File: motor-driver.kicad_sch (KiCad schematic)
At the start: 0 parts

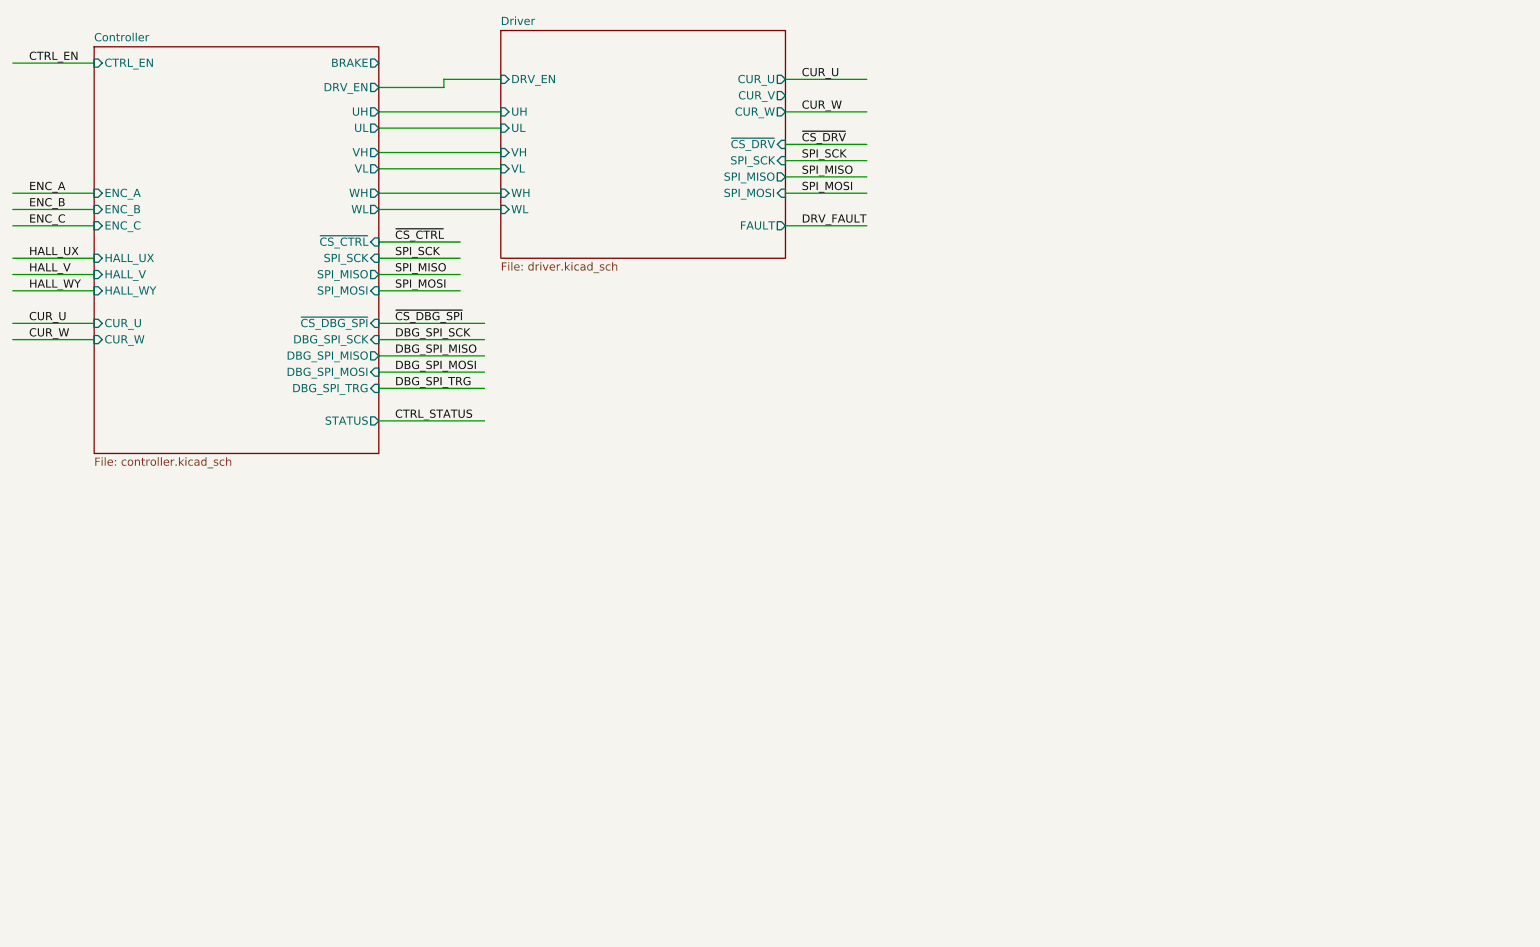
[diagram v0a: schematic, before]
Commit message: Add RTMI connector.
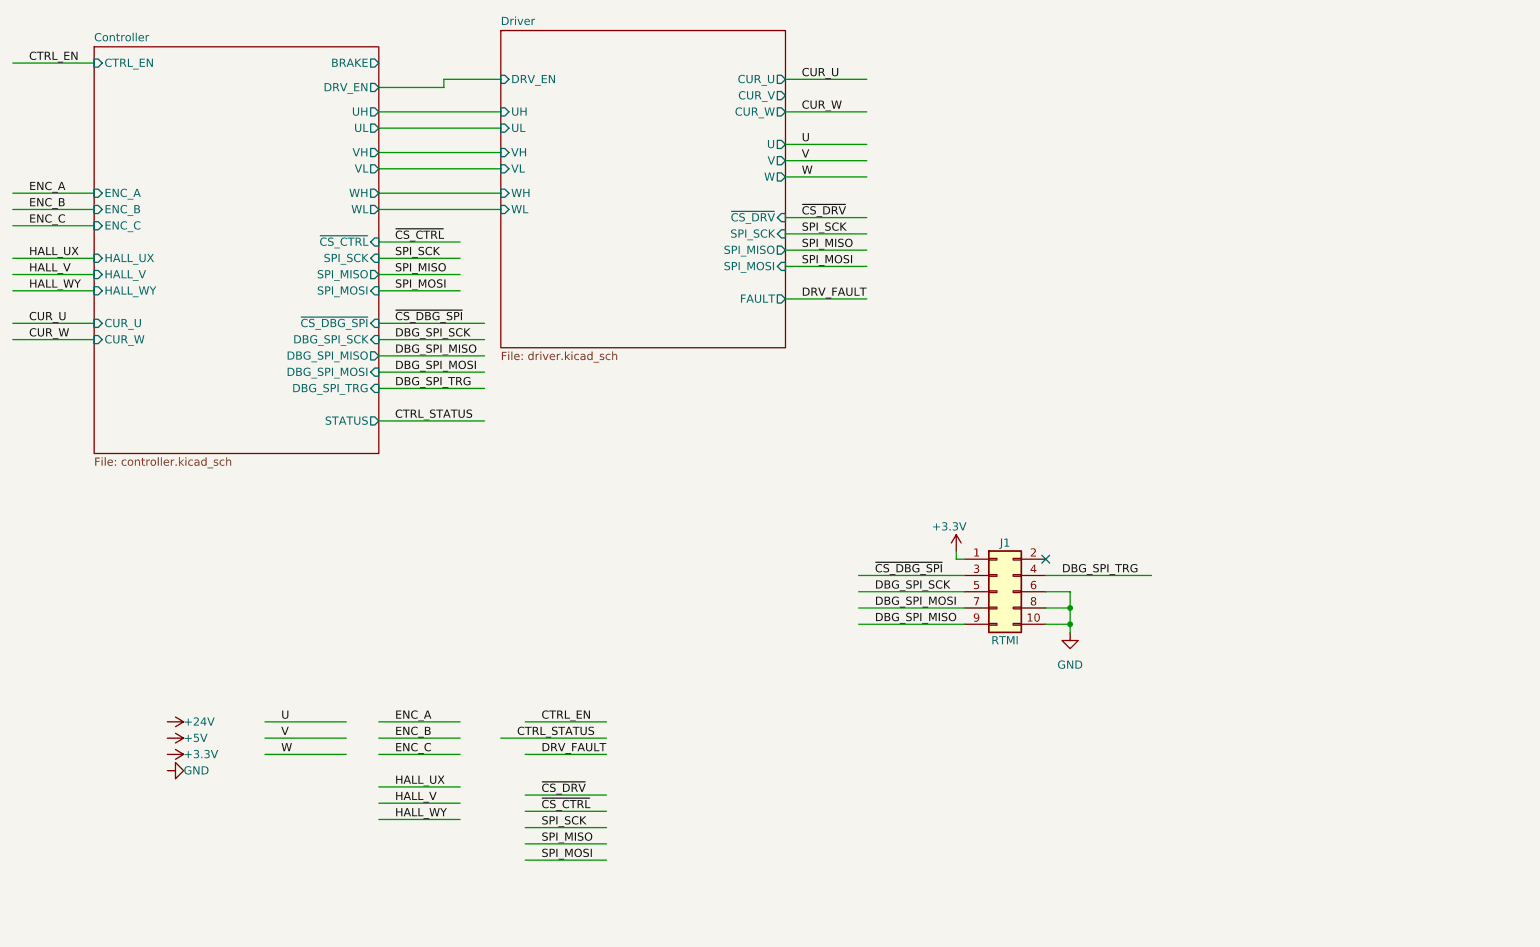
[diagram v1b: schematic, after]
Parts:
- added J1: RTMI, symbol Connector_Generic:Conn_02x05_Odd_Even
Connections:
- net DBG_SPI_MISO: now also J1.9 (Pin_9)
- net DBG_SPI_MOSI: now also J1.7 (Pin_7)
- net DBG_SPI_SCK: now also J1.5 (Pin_5)
- net DBG_SPI_TRG: now also J1.4 (Pin_4)
- net ~{CS_DBG_SPI}: now also J1.3 (Pin_3)
- new net +3.3V: J1.1 (Pin_1)
- new net GND: J1.10 (Pin_10), J1.6 (Pin_6), J1.8 (Pin_8)
- no-connect marks 0 -> 1
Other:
- sheet Driver ports: added U, V, W; removed none

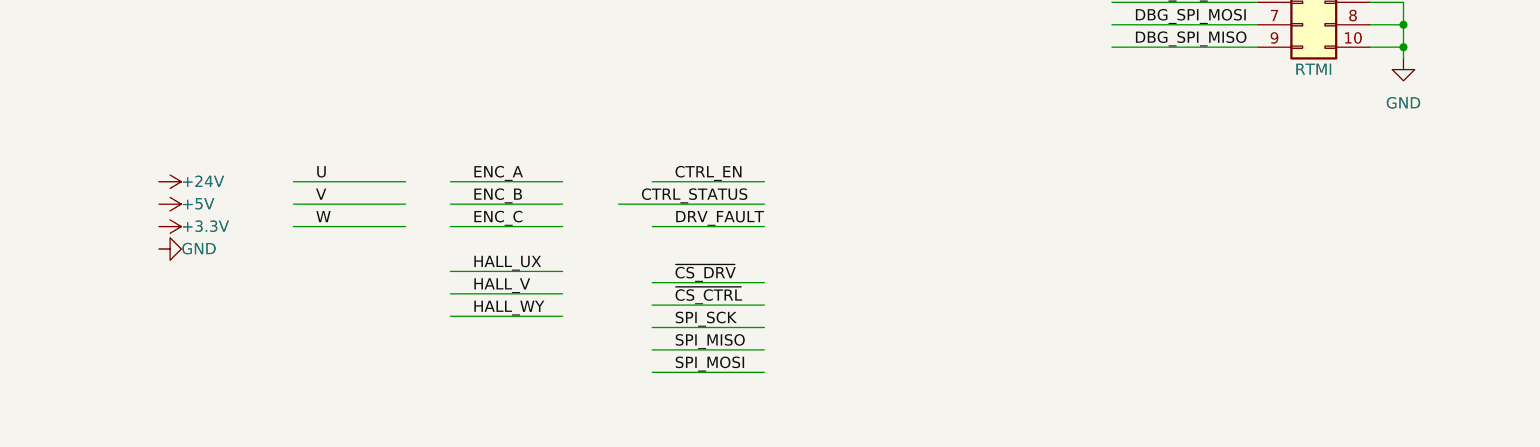
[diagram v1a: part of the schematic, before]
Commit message: Add stacking pin headers.
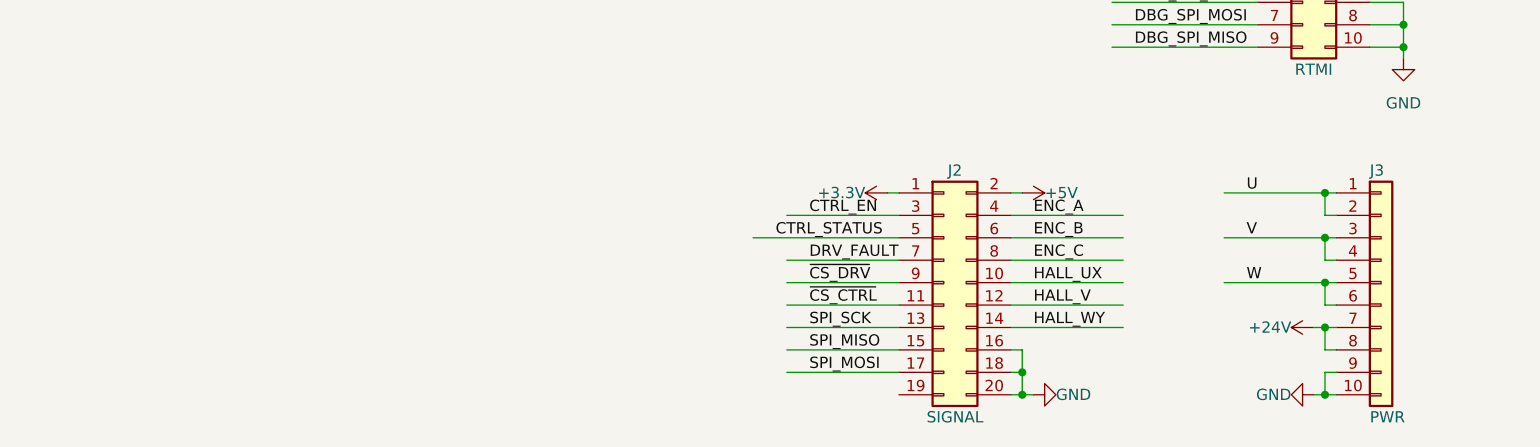
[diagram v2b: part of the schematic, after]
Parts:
- added J2: SIGNAL, Connector_PinHeader_2.54mm:PinHeader_2x10_P2.54mm_Vertical, symbol Connector_Generic:Conn_02x10_Odd_Even
- added J3: PWR, Connector_PinHeader_2.54mm:PinHeader_1x10_P2.54mm_Vertical, symbol Connector_Generic:Conn_01x10
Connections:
- net +24V: now also J3.7 (Pin_7), J3.8 (Pin_8)
- net +3.3V: now also J2.1 (Pin_1)
- net +5V: now also J2.2 (Pin_2)
- net CTRL_EN: now also J2.3 (Pin_3)
- net CTRL_STATUS: now also J2.5 (Pin_5)
- net DRV_FAULT: now also J2.7 (Pin_7)
- net ENC_A: now also J2.4 (Pin_4)
- net ENC_B: now also J2.6 (Pin_6)
- net ENC_C: now also J2.8 (Pin_8)
- net GND: now also J2.16 (Pin_16), J2.18 (Pin_18), J2.20 (Pin_20), J3.10 (Pin_10), J3.9 (Pin_9)
- net HALL_UX: now also J2.10 (Pin_10)
- net HALL_V: now also J2.12 (Pin_12)
- net HALL_WY: now also J2.14 (Pin_14)
- net SPI_MISO: now also J2.15 (Pin_15)
- net SPI_MOSI: now also J2.17 (Pin_17)
- net SPI_SCK: now also J2.13 (Pin_13)
- net U: now also J3.1 (Pin_1), J3.2 (Pin_2)
- net V: now also J3.3 (Pin_3), J3.4 (Pin_4)
- net W: now also J3.5 (Pin_5), J3.6 (Pin_6)
- net ~{CS_CTRL}: now also J2.11 (Pin_11)
- net ~{CS_DRV}: now also J2.9 (Pin_9)

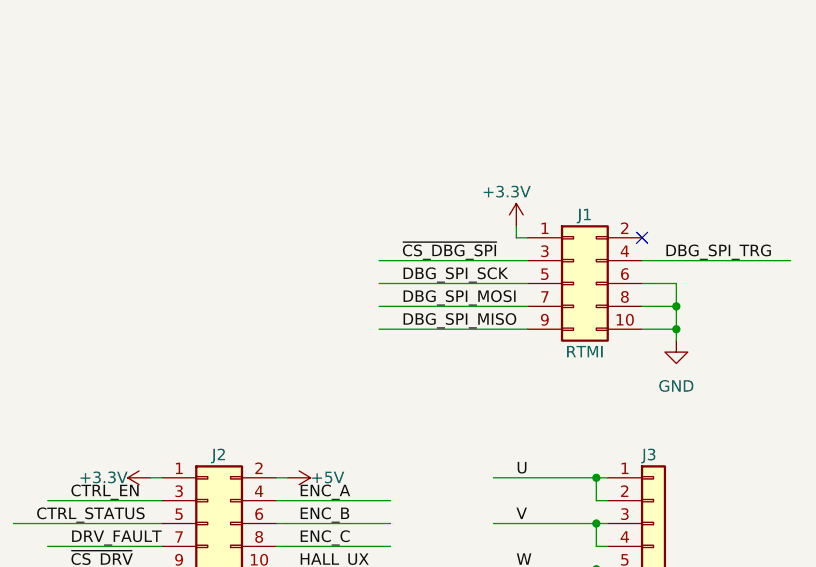
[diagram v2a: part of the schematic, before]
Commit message: Assign footprints and part numbers.
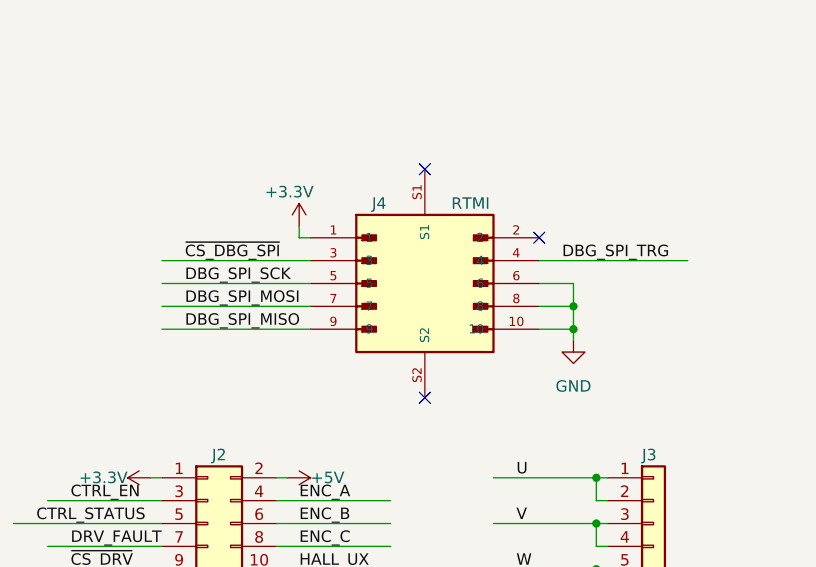
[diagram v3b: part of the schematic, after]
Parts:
- removed J1: RTMI, symbol Connector_Generic:Conn_02x05_Odd_Even
- added J4: RTMI, DF20EF-10DP-1V_52:HRS_DF20EF-10DP-1V(52), symbol DF20EF-10DP-1V_52_:DF20EF-10DP-1V(52)
- J2: MPN (none) -> 61302021121
- J3: MPN (none) -> 61301011121
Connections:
- net +3.3V: now also J4.1
- net DBG_SPI_MISO: now also J4.9
- net DBG_SPI_MOSI: now also J4.7
- net DBG_SPI_SCK: now also J4.5
- net DBG_SPI_TRG: now also J4.4
- net GND: now also J4.10, J4.6, J4.8
- net ~{CS_DBG_SPI}: now also J4.3
- no-connect marks 1 -> 3

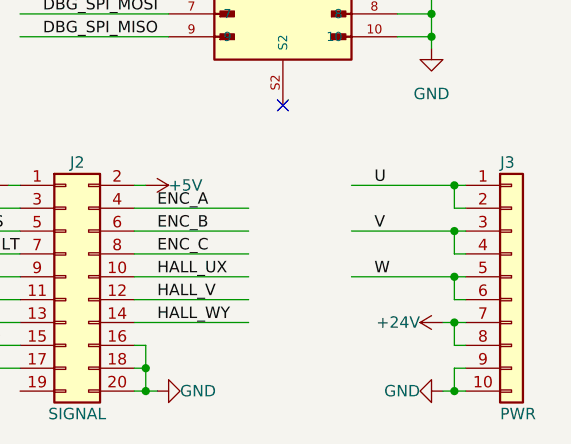
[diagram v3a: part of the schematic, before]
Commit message: Finish the initial placement, switch most of the parts to 0402.
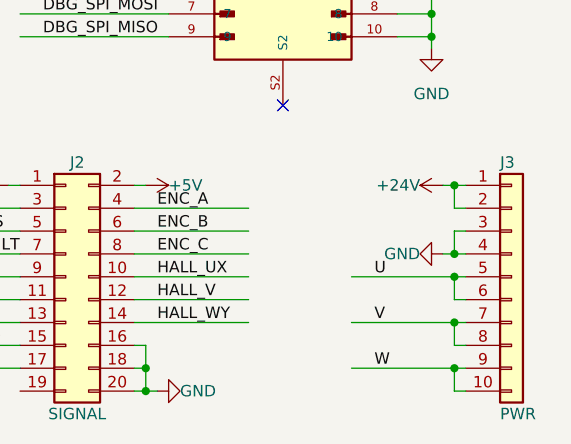
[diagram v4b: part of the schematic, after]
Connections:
- net +24V: now also J3.1 (Pin_1), J3.2 (Pin_2); no longer J3.7 (Pin_7), J3.8 (Pin_8)
- net GND: now also J3.3 (Pin_3), J3.4 (Pin_4); no longer J3.10 (Pin_10), J3.9 (Pin_9)
- net U: now also J3.5 (Pin_5), J3.6 (Pin_6); no longer J3.1 (Pin_1), J3.2 (Pin_2)
- net V: now also J3.7 (Pin_7), J3.8 (Pin_8); no longer J3.3 (Pin_3), J3.4 (Pin_4)
- net W: now also J3.10 (Pin_10), J3.9 (Pin_9); no longer J3.5 (Pin_5), J3.6 (Pin_6)

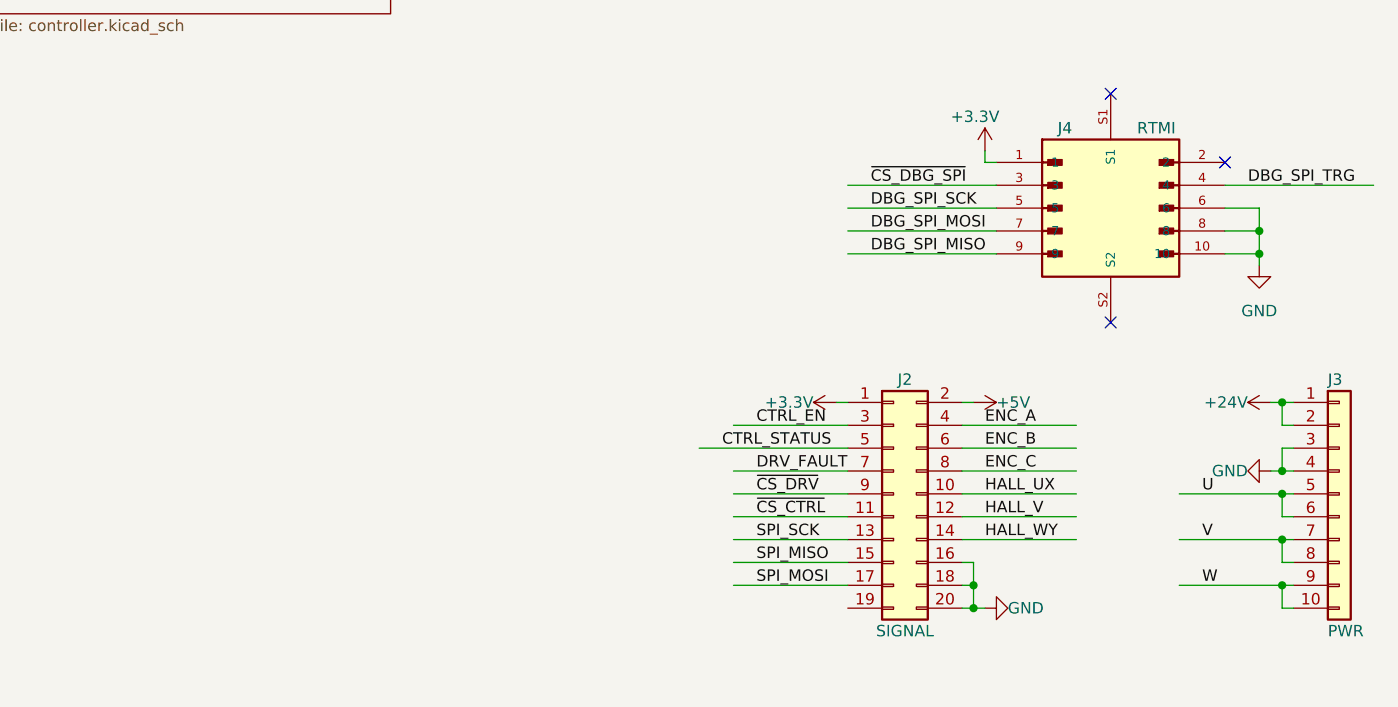
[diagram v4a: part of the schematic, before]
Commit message: Add signal RCs and debug LEDs.
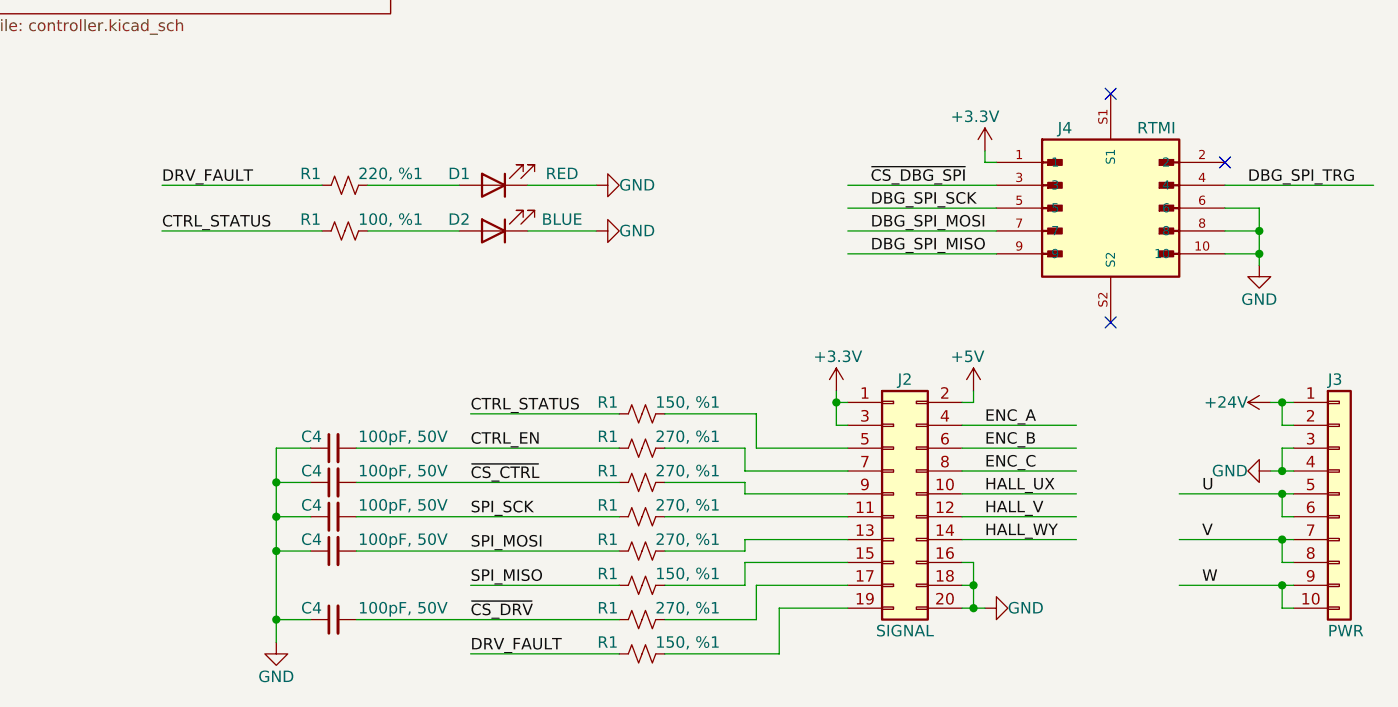
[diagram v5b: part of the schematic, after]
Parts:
- added C4 (x5): 100pF, 50V, Capacitor_SMD:C_0402_1005Metric, symbol Device:C_Small
- added D1: RED, LED_SMD:LED_0603_1608Metric, symbol Device:LED
- added D2: BLUE, LED_SMD:LED_0603_1608Metric, symbol Device:LED
- added R1: 100, %1, Resistor_SMD:R_0402_1005Metric, symbol Device:R_Small_US
- added R1 (x5): 270, %1, Resistor_SMD:R_0402_1005Metric, symbol Device:R_Small_US
- added R1 (x3): 150, %1, Resistor_SMD:R_0402_1005Metric, symbol Device:R_Small_US
- added R1: 220, %1, Resistor_SMD:R_0402_1005Metric, symbol Device:R_Small_US
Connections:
- net +3.3V: now also J2.3 (Pin_3)
- net CTRL_EN: now also C4.2, R1.1; no longer J2.3 (Pin_3)
- net CTRL_STATUS: now also R1.1, R1.1; no longer J2.5 (Pin_5)
- net DRV_FAULT: now also R1.1, R1.1; no longer J2.7 (Pin_7)
- net GND: now also C4.1, C4.1, C4.1, C4.1, C4.1, D1.1 (K), D2.1 (K)
- net SPI_MISO: now also R1.1; no longer J2.15 (Pin_15)
- net SPI_MOSI: now also C4.2, R1.1; no longer J2.17 (Pin_17)
- net SPI_SCK: now also C4.2, R1.1; no longer J2.13 (Pin_13)
- net ~{CS_CTRL}: now also C4.2, R1.1; no longer J2.11 (Pin_11)
- net ~{CS_DRV}: now also C4.2, R1.1; no longer J2.9 (Pin_9)
- net at J2.19 (Pin_19): now also R1.2
- new net: D2.2 (A), R1.2
- new net: J2.11 (Pin_11), R1.2
- new net: J2.9 (Pin_9), R1.2
- new net: J2.15 (Pin_15), R1.2
- new net: J2.13 (Pin_13), R1.2
- new net: D1.2 (A), R1.2
- new net: J2.7 (Pin_7), R1.2
- new net: J2.5 (Pin_5), R1.2
- new net: J2.17 (Pin_17), R1.2
